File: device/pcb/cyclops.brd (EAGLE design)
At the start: 124.5 x 79.9 mm, 187 parts, among them Q1 NDS351AN, Q2 NDS351AN, Q3 NDS351AN, Q4 IRF510, U1 MCP4921, U10 ADG1201, U11 THS4281, U12 MAX4564, U13 ZXTD, U14 ZXTD, U15 OPA1664, U16 LTM8020, U2 LT1931, U3 LT1764A, U4 BD00FC0WEFJ, U5 TPS72325, U6 LT1711, U7 TLV3701, U8 ADR03, U9 LT1880

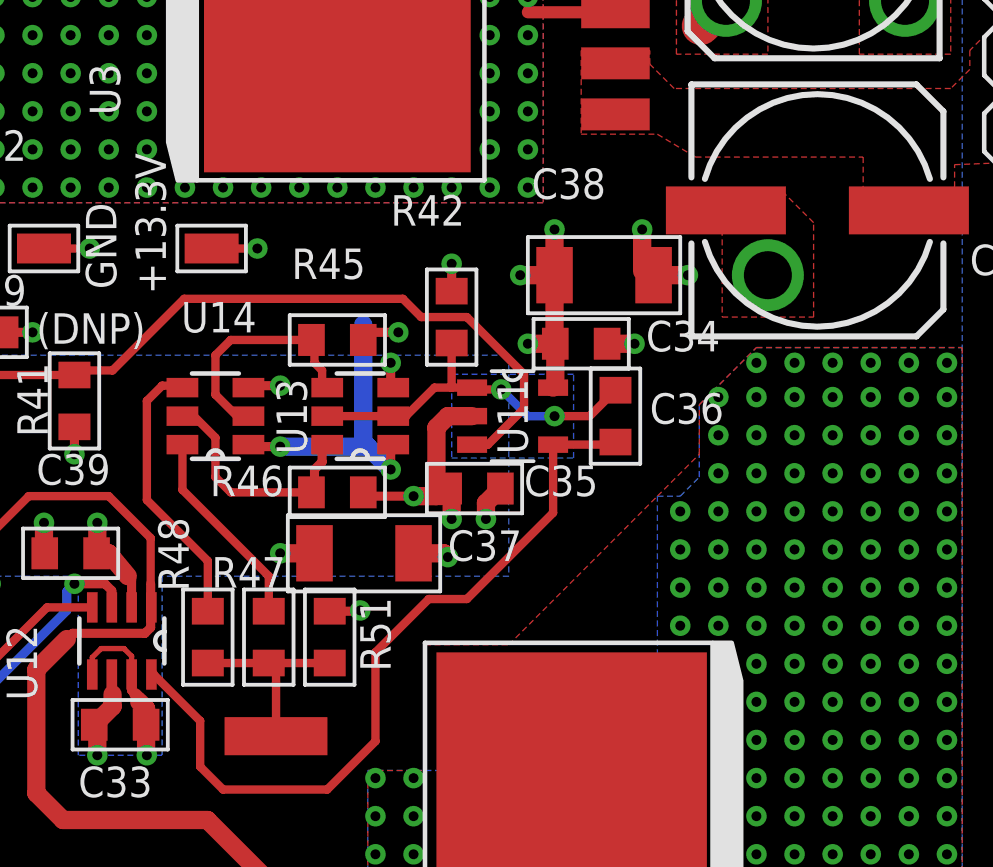
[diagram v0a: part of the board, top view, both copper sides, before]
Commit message: Stablized booster stage for high side LED.
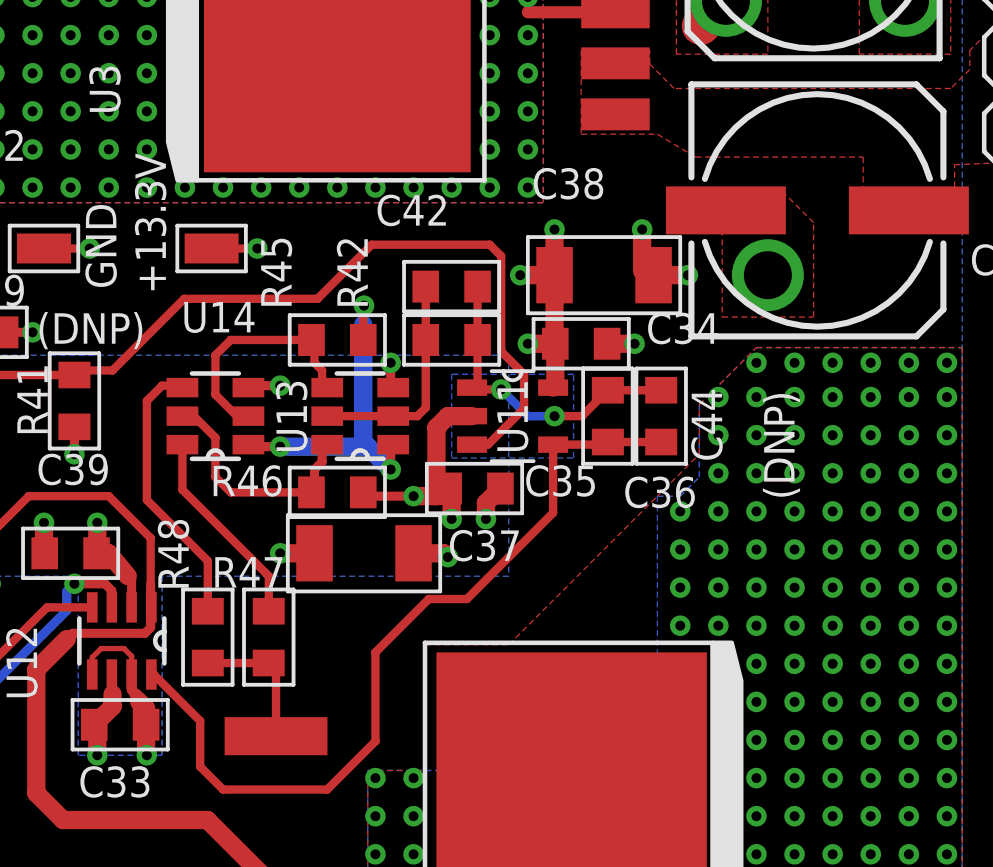
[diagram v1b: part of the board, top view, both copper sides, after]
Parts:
- removed R51: 10k, cyclops:0603
- added C42: 100pF, cyclops:0603
- added C44: 220pF, cyclops:0603
- R42: value 2.2k -> 50
- R45, R46: value 2.2k -> 1k
- moved R42 0.76 mm to (95.5, 46.2), turned to 180 degrees
- moved C36 0.25 mm to (100.7, 43.7)
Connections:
- new net N$16: C42.2, R42.2, U13.2, U13.5
- net COM: now also C44.1
- net GND: no longer R42.2, R51.1
- net N$13: now also C42.1, C44.2; no longer U13.2, U13.5
- net N$26: no longer R51.2
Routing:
- net N$16: track 0.00 -> 7.44 mm
- net _VREF: track 38.8 -> 42.1 mm
- net COM: track 25.8 -> 27.9 mm
- net N$26: track 6.60 -> 4.57 mm
- net GND: track 107.3 -> 105.3 mm, vias 419 -> 417
- net N$13: track 12.2 -> 10.5 mm

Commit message: Final circuit changes before production.
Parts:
- removed C26: .1uF, cyclops:0603
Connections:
- net GND: no longer C26.2
- net REF5.0: no longer C26.1
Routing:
- net GND: track 105.3 -> 104.0 mm, vias 417 -> 415
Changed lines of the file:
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@@
 <?xml version="1.0" encoding="utf-8"?>
 <!DOCTYPE eagle SYSTEM "eagle.dtd">
-<eagle version="6.6.0">
+<eagle version="6.5.0">
 <drawing>
 <settings>
@@
 <grid distance="0.005" unitdist="inch" unit="inch" style="lines" multiple="1" display="yes" altdistance="0.025" altunitdist="inch" altunit="inch"/>
 <layers>
-<layer number="1" name="Top" color="4" fill="1" visible="no" active="yes"/>
-<layer number="2" name="Route2" color="1" fill="3" visible="no" active="yes"/>
+<layer number="1" name="Top" color="4" fill="1" visible="yes" active="yes"/>
+<layer number="2" name="Route2" color="1" fill="3" visible="yes" active="yes"/>
 <layer number="3" name="Route3" color="4" fill="3" visible="no" active="no"/>
 <layer number="4" name="Route4" color="1" fill="4" visible="no" active="no"/>
@@
 <layer number="13" name="Route13" color="4" fill="5" visible="no" active="no"/>
 <layer number="14" name="Route14" color="1" fill="6" visible="no" active="no"/>
-<layer number="15" name="Route15" color="4" fill="6" visible="no" active="yes"/>
-<layer number="16" name="Bottom" color="1" fill="1" visible="no" active="yes"/>
+<layer number="15" name="Route15" color="4" fill="6" visible="yes" active="yes"/>
+<layer number="16" name="Bottom" color="1" fill="1" visible="yes" active="yes"/>
 <layer number="17" name="Pads" color="2" fill="1" visible="yes" active="yes"/>
 <layer number="18" name="Vias" color="2" fill="1" visible="yes" active="yes"/>
-<layer number="19" name="Unrouted" color="6" fill="1" visible="no" active="yes"/>
-<layer number="20" name="Dimension" color="15" fill="1" visible="no" active="yes"/>
+<layer number="19" name="Unrouted" color="6" fill="1" visible="yes" active="yes"/>
+<layer number="20" name="Dimension" color="15" fill="1" visible="yes" active="yes"/>
 <layer number="21" name="tPlace" color="7" fill="1" visible="yes" active="yes"/>
-<layer number="22" name="bPlace" color="7" fill="1" visible="no" active="yes"/>
+<layer number="22" name="bPlace" color="7" fill="1" visible="yes" active="yes"/>
 <layer number="23" name="tOrigins" color="15" fill="1" visible="yes" active="yes"/>
-<layer number="24" name="bOrigins" color="15" fill="1" visible="no" active="yes"/>
+<layer number="24" name="bOrigins" color="15" fill="1" visible="yes" active="yes"/>
 <layer number="25" name="tNames" color="7" fill="1" visible="yes" active="yes"/>
-<layer number="26" name="bNames" color="7" fill="1" visible="no" active="yes"/>
+<layer number="26" name="bNames" color="7" fill="1" visible="yes" active="yes"/>
 <layer number="27" name="tValues" color="7" fill="1" visible="yes" active="yes"/>
-<layer number="28" name="bValues" color="7" fill="1" visible="no" active="yes"/>
+<layer number="28" name="bValues" color="7" fill="1" visible="yes" active="yes"/>
 <layer number="29" name="tStop" color="7" fill="3" visible="yes" active="yes"/>
-<layer number="30" name="bStop" color="7" fill="6" visible="no" active="yes"/>
+<layer number="30" name="bStop" color="7" fill="6" visible="yes" active="yes"/>
 <layer number="31" name="tCream" color="7" fill="4" visible="no" active="yes"/>
 <layer number="32" name="bCream" color="7" fill="5" visible="no" active="yes"/>
@@
 <text x="74.295" y="83.566" size="1.016" layer="21" font="vector" ratio="18" rot="R90">VCTL or CONT</text>
 <text x="106.934" y="40.894" size="1.016" layer="21" font="vector" ratio="18" rot="R90">(DNP)</text>
+<text x="3.429" y="4.572" size="1.016" layer="21" font="vector" ratio="18" rot="R270" align="center">DGND</text>
+<text x="33.909" y="69.977" size="1.016" layer="21" font="vector" ratio="18" rot="R180" align="center">GND</text>
+<text x="73.152" y="33.909" size="1.016" layer="21" font="vector" ratio="18" rot="R180" align="center">GND</text>
+<text x="88.773" y="67.691" size="1.016" layer="21" font="vector" ratio="18" rot="R180" align="center">GND</text>
+<text x="58.039" y="67.437" size="1.016" layer="21" font="vector" ratio="18" rot="R180" align="center">GND</text>
+<text x="14.351" y="70.866" size="1.016" layer="21" font="vector" ratio="18" rot="R270" align="center">GND</text>
 </plain>
 <attributes>
@@
 <attribute name="VALUE" x="60.452" y="59.944" size="1.016" layer="27" font="vector" ratio="18" rot="R180" align="center-left"/>
 </element>
-<element name="C26" library="cyclops" package="0603" value=".1uF" x="62.23" y="63.5" smashed="yes">
-<attribute name="NAME" x="60.96" y="66.294" size="1.016" layer="25" font="vector" ratio="18" rot="R180" align="center-right"/>
-<attribute name="VALUE" x="60.96" y="65.151" size="1.016" layer="27" font="vector" ratio="18" align="center-left"/>
-</element>
 <element name="U$30" library="open-ephys" package="OPEN_EPHYS_LOGO" value="OPEN_EPHYS_LOGO" x="65.568446875" y="24.59875625" smashed="yes" rot="MR315"/>
 <element name="HEATSINK" library="jonnew" package="BDN17" value="BDN17" x="112.522" y="20.193" smashed="yes" rot="MR0">
@@
 </element>
 <element name="-2.5V" library="jonnew" package="RC0603" value="RCU-0C" x="60.325" y="28.194" smashed="yes" rot="R180">
-<attribute name="NAME" x="61.1759" y="27.5199" size="1.016" layer="25" font="vector" ratio="18"/>
+<attribute name="NAME" x="62.7771" y="25.8699" size="1.016" layer="25" font="vector" ratio="18" rot="R90"/>
 </element>
 <element name="VPRE" library="jonnew" package="RC0603" value="TPTP16R" x="48.133" y="61.722" smashed="yes" rot="R90">
@@
 <via x="25.019" y="56.007" extent="1-16" drill="0.6"/>
 <contactref element="R33" pad="2"/>
-<contactref element="C26" pad="2"/>
-<via x="62.738" y="62.357" extent="1-16" drill="0.3302"/>
 <contactref element="R44" pad="2"/>
 <wire x1="61.8744" y1="52.19" x2="61.856" y2="52.19" width="0.3048" layer="1"/>
@@
 <via x="39.624" y="15.494" extent="1-16" drill="0.3302"/>
 <wire x1="39.624" y1="14.373" x2="39.624" y2="15.494" width="0.2794" layer="1"/>
-<wire x1="63.0936" y1="63.5" x2="63.119" y2="63.4746" width="0.2794" layer="1"/>
 <via x="50.927" y="42.545" extent="1-16" drill="0.3302"/>
 <wire x1="49.972" y1="42.477" x2="50.859" y2="42.477" width="0.2794" layer="1"/>
@@
 <via x="16.764" y="1.524" extent="1-16" drill="0.3302"/>
 <via x="11.303" y="1.016" extent="1-16" drill="0.3302"/>
-<via x="3.429" y="1.905" extent="1-16" drill="0.3302"/>
 <via x="4.318" y="6.35" extent="1-16" drill="0.3302"/>
 <via x="2.413" y="8.763" extent="1-16" drill="0.3302"/>
@@
 <via x="28.702" y="31.623" extent="1-16" drill="0.3302"/>
 <via x="27.813" y="30.607" extent="1-16" drill="0.3302"/>
-<wire x1="63.119" y1="63.4746" x2="62.738" y2="63.0936" width="0.2794" layer="1"/>
-<wire x1="62.738" y1="63.0936" x2="62.738" y2="62.357" width="0.2794" layer="1"/>
 <contactref element="OC" pad="C2"/>
 <contactref element="R29" pad="1"/>
@@
 <wire x1="52.707" y1="72.388" x2="52.707" y2="72.223" width="0.3048" layer="1"/>
 <contactref element="R34" pad="1"/>
-<contactref element="C26" pad="1"/>
 <contactref element="REF5V0" pad="1"/>
-<wire x1="61.3664" y1="63.5" x2="61.3664" y2="63.4746" width="0.3048" layer="1"/>
 <contactref element="R18" pad="2"/>
 <contactref element="R17" pad="1"/>
@@
 <wire x1="51.435" y1="57.023" x2="51.435" y2="52.832" width="0.2794" layer="1"/>
 <wire x1="61.468" y1="61.3156" x2="61.3664" y2="61.3156" width="0.6096" layer="1"/>
-<wire x1="61.3664" y1="61.3156" x2="61.3664" y2="63.5" width="0.6096" layer="1"/>
 <wire x1="52.707" y1="72.223" x2="52.707" y2="72.1594" width="0.6096" layer="1"/>
-<wire x1="52.707" y1="72.1594" x2="61.3664" y2="63.5" width="0.6096" layer="1"/>
 <wire x1="59.5376" y1="40.513" x2="59.817" y2="40.7924" width="0.6096" layer="1"/>
 <wire x1="59.817" y1="40.7924" x2="59.817" y2="46.1251" width="0.6096" layer="1"/>
@@
 <wire x1="63.881" y1="62.611" x2="71.12" y2="69.85" width="0.6096" layer="1"/>
 <wire x1="71.12" y1="69.85" x2="72.6694" y2="69.85" width="0.6096" layer="1"/>
+<wire x1="52.707" y1="72.1594" x2="53.3166" y2="72.1594" width="0.6096" layer="1"/>
+<wire x1="53.3166" y1="72.1594" x2="61.468" y2="64.008" width="0.6096" layer="1"/>
+<wire x1="61.468" y1="64.008" x2="61.468" y2="61.3156" width="0.6096" layer="1"/>
 </signal>
 <signal name="N$3">
@@
 <wire x1="94.6404" y1="43.9674" x2="94.361" y2="43.688" width="0.2794" layer="1"/>
 </signal>
+<signal name="GND1">
+<via x="3.429" y="1.524" extent="1-16" drill="1.1" shape="octagon" alwaysstop="yes"/>
+</signal>
+<signal name="GND2">
+<via x="31.242" y="69.977" extent="1-16" drill="1.1" shape="octagon" alwaysstop="yes"/>
+</signal>
+<signal name="GND3">
+<via x="70.485" y="33.909" extent="1-16" drill="1.1" shape="octagon" alwaysstop="yes"/>
+</signal>
+<signal name="GND4">
+<via x="86.106" y="67.691" extent="1-16" drill="1.1" shape="octagon" alwaysstop="yes"/>
+</signal>
+<signal name="GND5">
+<via x="55.499" y="67.437" extent="1-16" drill="1.1" shape="octagon" alwaysstop="yes"/>
+</signal>
+<signal name="GND6">
+<via x="14.351" y="68.199" extent="1-16" drill="1.1" shape="octagon" alwaysstop="yes"/>
+</signal>
 </signals>

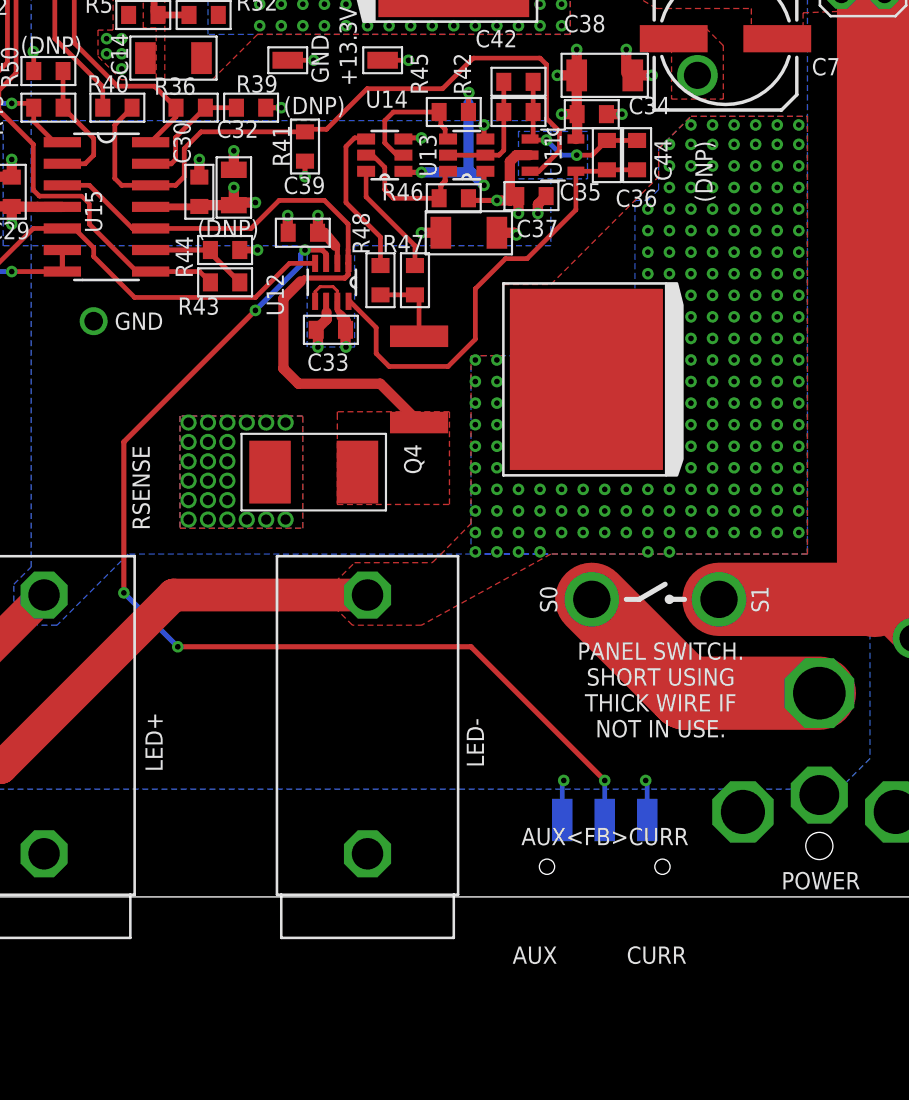
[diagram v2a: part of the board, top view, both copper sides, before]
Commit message: Added bandwidth limit selection
- Added analog switch to insert 6.8nF of compensation capacitance into
  the current sense feedback loop for when people use long cables or
  slow transimpedance photodiode amplifiers
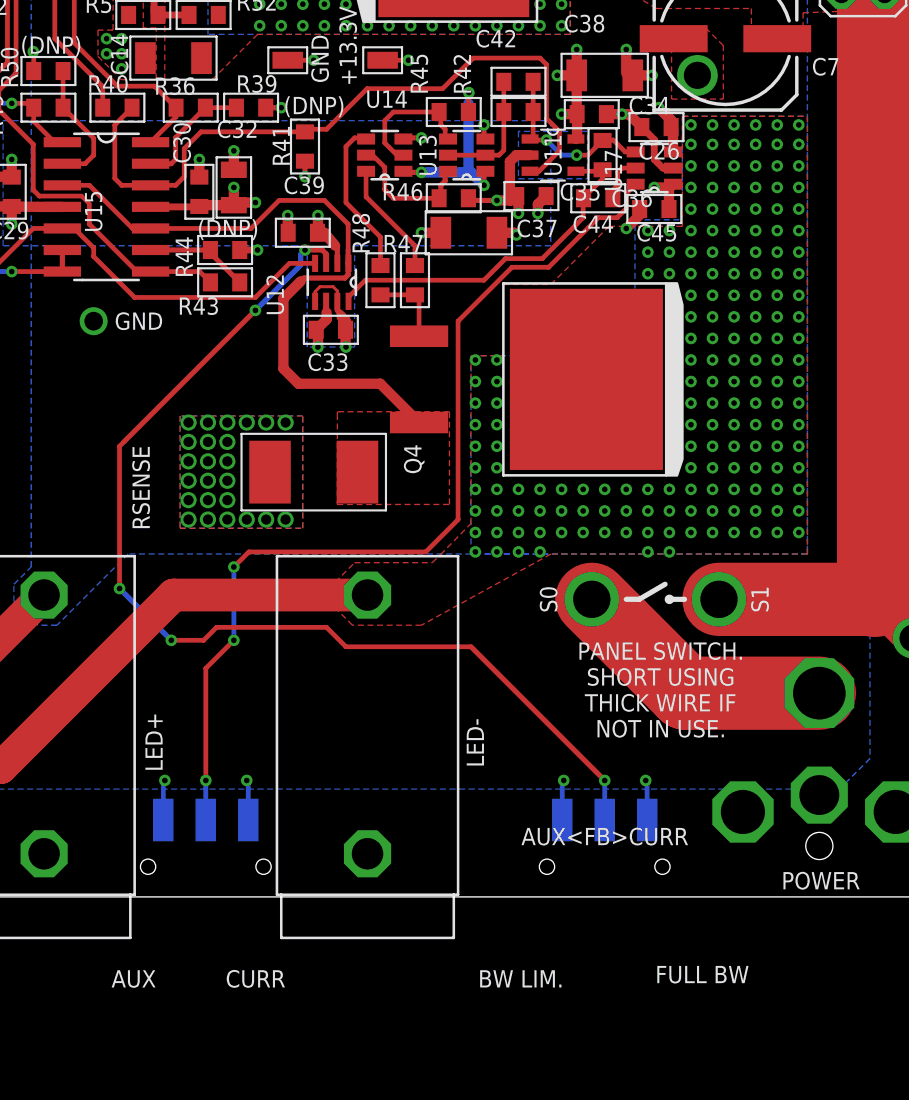
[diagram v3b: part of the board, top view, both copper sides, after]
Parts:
- added BWFULL<>BWLIM: JS102, cyclops:JS102011SAQN
- added C26, C45: 0.1uF, cyclops:0603
- added U17: DG9421, jonnew:SOT23-6
- C44: value 220pF -> 6.8nF
- R38: value 2.2k -> 2.1k
- U10: value ADG1201 -> DG9421
- moved C44 3.42 mm to (100.2, 41.1), turned to 0 degrees
- moved C36 0.25 mm to (100.5, 43.7)
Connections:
- new net IN1: BWFULL<>BWLIM.2, U17.6
- new net N$40: C44.2, U17.5
- net +6V: now also BWFULL<>BWLIM.3, C45.1, U17.1
- net -2.5V: now also C26.1, U17.3
- net GND: now also BWFULL<>BWLIM.1, C26.2, C45.2, U17.2
- net N$13: now also U17.4; no longer C44.2
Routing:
- net IN1: track 0.00 -> 56.0 mm, vias 0 -> 3
- net GND: track 104.0 -> 112.5 mm, vias 415 -> 417
- net COM: track 27.9 -> 20.9 mm
- net +6V: track 59.7 -> 64.8 mm, vias 30 -> 32
- net -2.5V: track 33.4 -> 36.4 mm, vias 26 -> 27
- net N$40: track 0.00 -> 2.80 mm
- net IN: track 61.7 -> 62.6 mm
- net LED-: vias 180 -> 175
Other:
- board text added: "BW LIM."
- board text added: "FULL BW"
